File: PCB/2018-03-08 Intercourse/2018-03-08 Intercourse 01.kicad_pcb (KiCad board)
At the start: 2 copper layers, 85.6 x 54 mm, 50 parts, among them J1 USB_C_Receptacle, J2 TP_RST, J3 TP_TX, J4 TP_RX, J5 TP_GPIO0, J6 TP_GND1, J7 TP_GND2, J8 TP_GND3, U1 LTC3225, U2 TPS61221DCKR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

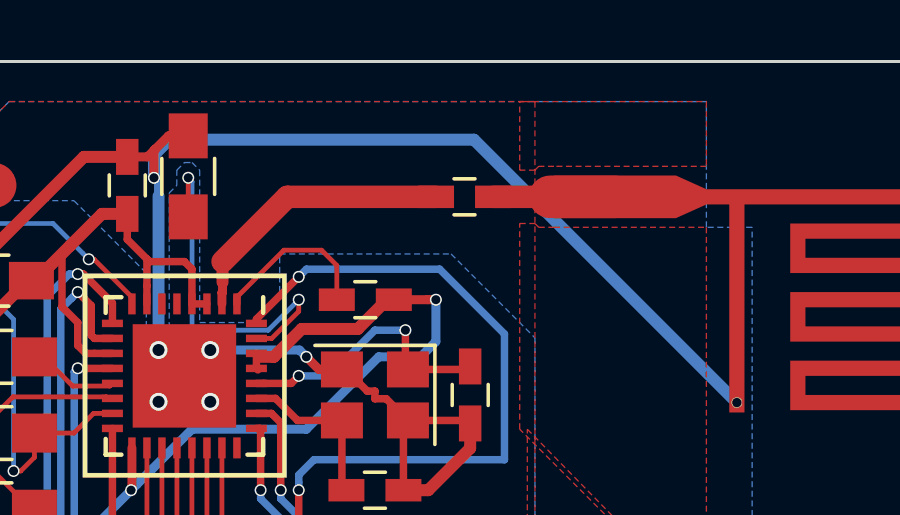
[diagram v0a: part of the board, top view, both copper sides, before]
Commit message: rev4 ready for review
- added parts to antenna trace
- created gerber files
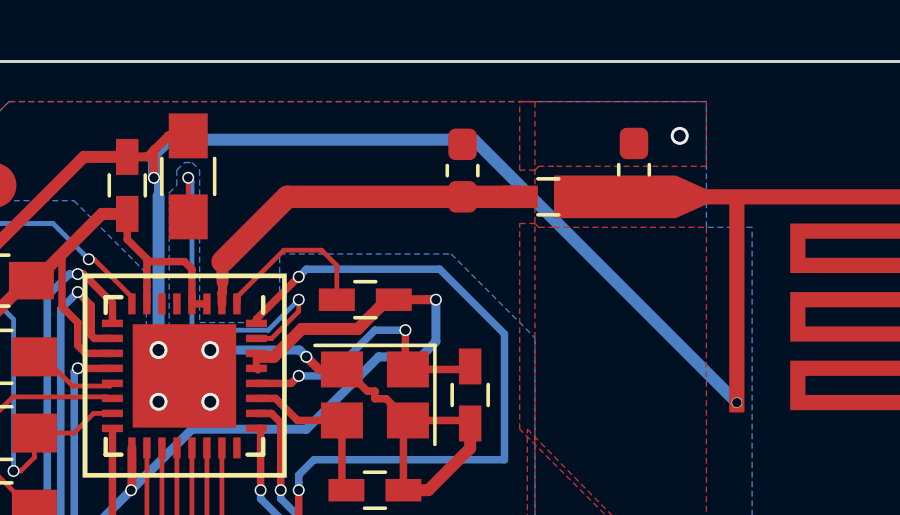
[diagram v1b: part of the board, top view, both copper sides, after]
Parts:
- added C13: ?, Capacitor_SMD:C_0603_1608Metric_Pad1.05x0.95mm_HandSolder, F.Cu at (177.5, 78.2)
- added C14: ?, Capacitor_SMD:C_0603_1608Metric_Pad1.05x0.95mm_HandSolder, F.Cu at (171.8, 78.2)
- moved C10 2.79 mm to (174.7, 79.1), turned to 0 degrees
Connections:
- C10 pad 1: Net-(AE1-Pad2) -> Net-(C10-Pad1)
- C10 pad 2: Net-(C10-Pad2) -> Net-(AE1-Pad2)
- U4 pad 2: Net-(C10-Pad2) -> Net-(C10-Pad1)
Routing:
- net Net-(C10-Pad1): track 0.00 -> 12.2 mm
- net Net-(C10-Pad2): track 10.4 -> 0.00 mm
- net Net-(AE1-Pad2): track 4.06 -> 0.00 mm
- net GND: vias 12 -> 13
